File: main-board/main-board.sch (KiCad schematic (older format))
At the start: 68 parts, among them J1 NVIDIA_Jetson_NX_Dev_40pin_Co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, J10 FSESC_6.6_COMM_Minimal, J11 FSESC_6.6_COMM_Minimal, J12 FSESC_6.6_COMM_Minimal, J13 FSESC_6.6_COMM_Minimal, J2 NVIDIA_Jetson_NX_Dev_Button_C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, J3 Conn_01x02, J4 Conn_01x02, J5 Conn_01x02, J6 FSESC_6.6_COMM_Minimal, J7 QWIIC_Generic_Conn, J8 Conn_01x03, J9 FSESC_6.6_COMM_Minimal, M1 Fan_3pin, M2 Fan_3pin, M3 Fan_3pin, Q1 Q_NMOS_GSD, Q2 Q_NMOS_GSD, Q4 Q_NMOS_GSD, Q5 Q_NMOS_GSD, Q6 Q_NMOS_GSD, Q7 Q_NMOS_GSD, Q8 Q_NMOS_GSD, U1 RFM95W_Adafruit_Breakout, U10 Analog Temp Sensor, U11 Adafruit_GPS_V3, U12 SN74AHCT125D, U2 TDK_I3A4W008A033V, U3 TDK_I3A4W008A033V, U5 Teensy_4.1, U6 Analog Temp Sensor, U7 Analog Temp Sensor, U8 Analog Temp Sensor, U9 Analog Temp Sensor

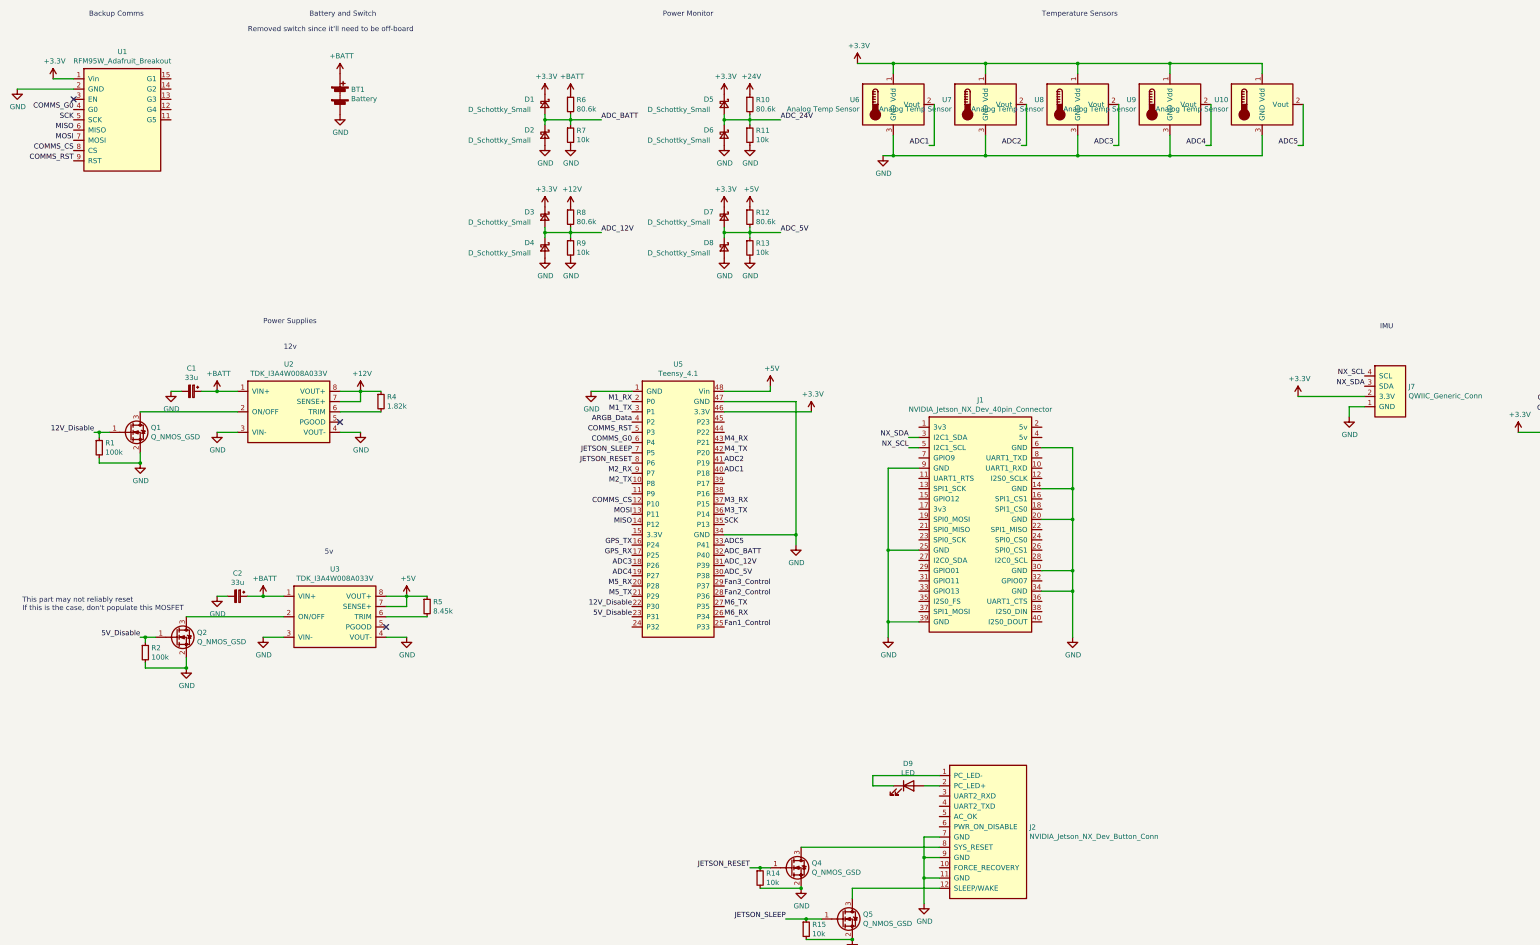
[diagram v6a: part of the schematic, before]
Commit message: Worked on PCB layout
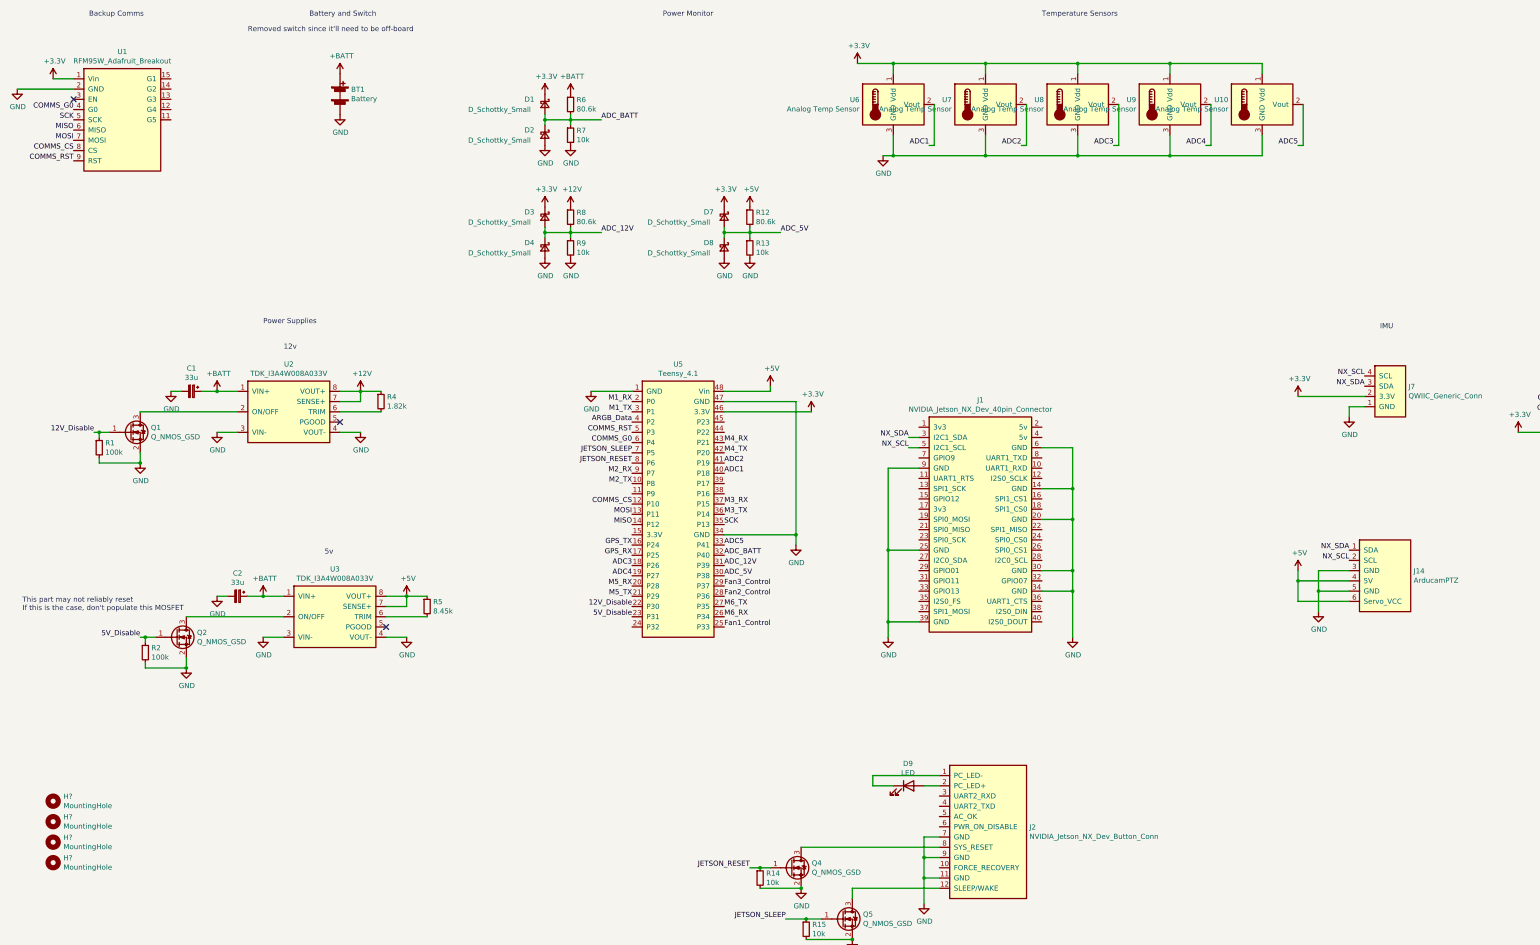
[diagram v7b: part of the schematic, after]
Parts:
- removed D5, D6: D_Schottky_Small, Diode_SMD:D_SOD-323_HandSoldering, symbol Device:D_Schottky_Small
- removed R10: 80.6k, Resistor_SMD:R_0603_1608Metric, symbol Device:R_Small
- removed R11: 10k, Resistor_SMD:R_0603_1608Metric, symbol Device:R_Small
- added H? (x4): MountingHole, MountingHole:MountingHole_3.2mm_M3, symbol Mechanical:MountingHole
- added J14: ArducamPTZ, Connector_JST:JST_XH_B6B-XH-A_1x06_P2.50mm_Vertical, symbol ASTRA_Library:ArducamPTZ
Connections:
- net +5V: now also J14.4 (5V), J14.6 (Servo_VCC)
- net GND: now also J14.3 (GND), J14.5 (GND)
- net NX_SCL: now also J14.2 (SCL)
- net NX_SDA: now also J14.1 (SDA)
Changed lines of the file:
@@
 Wire Wire Line
 	19900 13800 19900 13900
-Text Label 8050 2150 0    50   ~ 0
-ADC_24V
-$Comp
-L Device:R_Small R11
-U 1 1 6119C6A9
-P 7750 2300
-F 0 "R11" H 7809 2346 50  0000 L CNN
-F 1 "10k" H 7809 2255 50  0000 L CNN
-F 2 "Resistor_SMD:R_0603_1608Metric" H 7750 2300 50  0001 C CNN
-F 3 "~" H 7750 2300 50  0001 C CNN
-F 4 "311-10.0KHRCT-ND" H 7750 2300 50  0001 C CNN "Digikey Part Num"
-	1    7750 2300
-	1    0    0    -1
-$EndComp
-$Comp
-L Device:R_Small R10
-U 1 1 6119C6B4
-P 7750 2000
-F 0 "R10" H 7809 2046 50  0000 L CNN
-F 1 "80.6k" H 7809 1955 50  0000 L CNN
-F 2 "Resistor_SMD:R_0603_1608Metric" H 7750 2000 50  0001 C CNN
-F 3 "~" H 7750 2000 50  0001 C CNN
-F 4 "P20500CT-ND" H 7750 2000 50  0001 C CNN "Digikey Part Num"
-	1    7750 2000
-	1    0    0    -1
-$EndComp
-Wire Wire Line
-	8050 2150 7750 2150
-Wire Wire Line
-	7750 2150 7750 2100
-Wire Wire Line
-	7750 2150 7750 2200
-Connection ~ 7750 2150
-$Comp
-L Device:D_Schottky_Small D5
-U 1 1 6119C6C3
-P 7500 2000
-F 0 "D5" V 7450 1800 50  0000 L CNN
-F 1 "D_Schottky_Small" V 7550 1250 50  0000 L CNN
-F 2 "Diode_SMD:D_SOD-323_HandSoldering" V 7500 2000 50  0001 C CNN
-F 3 "~" V 7500 2000 50  0001 C CNN
-F 4 "1514-CMDD6001TRPBFREECT-ND" H 7500 2000 50  0001 C CNN "Digikey Part Num"
-	1    7500 2000
-	0    1    1    0
-$EndComp
-$Comp
-L Device:D_Schottky_Small D6
-U 1 1 6119C6CE
-P 7500 2300
-F 0 "D6" V 7450 2100 50  0000 L CNN
-F 1 "D_Schottky_Small" V 7550 1550 50  0000 L CNN
-F 2 "Diode_SMD:D_SOD-323_HandSoldering" V 7500 2300 50  0001 C CNN
-F 3 "~" V 7500 2300 50  0001 C CNN
-F 4 "1514-CMDD6001TRPBFREECT-ND" H 7500 2300 50  0001 C CNN "Digikey Part Num"
-	1    7500 2300
-	0    1    1    0
-$EndComp
-Wire Wire Line
-	7500 2100 7500 2150
-Wire Wire Line
-	7500 2150 7750 2150
-Wire Wire Line
-	7500 2200 7500 2150
-Connection ~ 7500 2150
-$Comp
-L power:GND #PWR038
-U 1 1 6119C6DC
-P 7750 2400
-F 0 "#PWR038" H 7750 2150 50  0001 C CNN
-F 1 "GND" H 7755 2227 50  0000 C CNN
-F 2 "" H 7750 2400 50  0001 C CNN
-F 3 "" H 7750 2400 50  0001 C CNN
-	1    7750 2400
-	1    0    0    -1
-$EndComp
-$Comp
-L power:GND #PWR034
-U 1 1 6119C6E6
-P 7500 2400
-F 0 "#PWR034" H 7500 2150 50  0001 C CNN
-F 1 "GND" H 7505 2227 50  0000 C CNN
-F 2 "" H 7500 2400 50  0001 C CNN
-F 3 "" H 7500 2400 50  0001 C CNN
-	1    7500 2400
-	1    0    0    -1
-$EndComp
-$Comp
-L power:+3.3V #PWR033
-U 1 1 6119C6F0
-P 7500 1900
-F 0 "#PWR033" H 7500 1750 50  0001 C CNN
-F 1 "+3.3V" H 7515 2073 50  0000 C CNN
-F 2 "" H 7500 1900 50  0001 C CNN
-F 3 "" H 7500 1900 50  0001 C CNN
-	1    7500 1900
-	1    0    0    -1
-$EndComp
-$Comp
-L power:+24V #PWR037
-U 1 1 611B45F0
-P 7750 1900
-F 0 "#PWR037" H 7750 1750 50  0001 C CNN
-F 1 "+24V" H 7765 2073 50  0000 C CNN
-F 2 "" H 7750 1900 50  0001 C CNN
-F 3 "" H 7750 1900 50  0001 C CNN
-	1    7750 1900
-	1    0    0    -1
-$EndComp
 $Comp
 L power:+5V #PWR06
@@
 	1    0    0    -1
 $EndComp
+$Comp
+L ASTRA_Library:ArducamPTZ J14
+U 1 1 612E83D2
+P 13950 6600
+F 0 "J14" H 14228 6646 50  0000 L CNN
+F 1 "ArducamPTZ" H 14228 6555 50  0000 L CNN
+F 2 "Connector_JST:JST_XH_B6B-XH-A_1x06_P2.50mm_Vertical" H 13600 6950 50  0001 C CNN
+F 3 "" H 13600 6950 50  0001 C CNN
+	1    13950 6600
+	1    0    0    -1
+$EndComp
+Text Label 13600 6350 2    50   ~ 0
+NX_SDA
+Text Label 13600 6450 2    50   ~ 0
+NX_SCL
+$Comp
+L power:GND #PWR0101
+U 1 1 612E9CF6
+P 13300 6950
+F 0 "#PWR0101" H 13300 6700 50  0001 C CNN
+F 1 "GND" H 13305 6777 50  0000 C CNN
+F 2 "" H 13300 6950 50  0001 C CNN
+F 3 "" H 13300 6950 50  0001 C CNN
+	1    13300 6950
+	1    0    0    -1
+$EndComp
+$Comp
+L power:+5V #PWR0102
+U 1 1 612FA1AA
+P 13100 6550
+F 0 "#PWR0102" H 13100 6400 50  0001 C CNN
+F 1 "+5V" H 13115 6723 50  0000 C CNN
+F 2 "" H 13100 6550 50  0001 C CNN
+F 3 "" H 13100 6550 50  0001 C CNN
+	1    13100 6550
+	1    0    0    -1
+$EndComp
+Wire Wire Line
+	13300 6950 13300 6750
+Wire Wire Line
+	13300 6550 13600 6550
+Wire Wire Line
+	13600 6650 13100 6650
+Wire Wire Line
+	13100 6650 13100 6550
+Wire Wire Line
+	13600 6850 13100 6850
+Wire Wire Line
+	13100 6850 13100 6650
+Connection ~ 13100 6650
+Wire Wire Line
+	13600 6750 13300 6750
+Connection ~ 13300 6750
+Wire Wire Line
+	13300 6750 13300 6550
+$Comp
+L Mechanical:MountingHole H?
+U 1 1 614879F3
+P 950 8800
+F 0 "H?" H 1050 8846 50  0000 L CNN
+F 1 "MountingHole" H 1050 8755 50  0000 L CNN
+F 2 "MountingHole:MountingHole_3.2mm_M3" H 950 8800 50  0001 C CNN
+F 3 "~" H 950 8800 50  0001 C CNN
+	1    950  8800
+	1    0    0    -1
+$EndComp
+$Comp
+L Mechanical:MountingHole H?
+U 1 1 6148830E
+P 950 9000
+F 0 "H?" H 1050 9046 50  0000 L CNN
+F 1 "MountingHole" H 1050 8955 50  0000 L CNN
+F 2 "MountingHole:MountingHole_3.2mm_M3" H 950 9000 50  0001 C CNN
+F 3 "~" H 950 9000 50  0001 C CNN
+	1    950  9000
+	1    0    0    -1
+$EndComp
+$Comp
+L Mechanical:MountingHole H?
+U 1 1 61488718
+P 950 9200
+F 0 "H?" H 1050 9246 50  0000 L CNN
+F 1 "MountingHole" H 1050 9155 50  0000 L CNN
+F 2 "MountingHole:MountingHole_3.2mm_M3" H 950 9200 50  0001 C CNN
+F 3 "~" H 950 9200 50  0001 C CNN
+	1    950  9200
+	1    0    0    -1
+$EndComp
+$Comp
+L Mechanical:MountingHole H?
+U 1 1 61488957
+P 950 9400
+F 0 "H?" H 1050 9446 50  0000 L CNN
+F 1 "MountingHole" H 1050 9355 50  0000 L CNN
+F 2 "MountingHole:MountingHole_3.2mm_M3" H 950 9400 50  0001 C CNN
+F 3 "~" H 950 9400 50  0001 C CNN
+	1    950  9400
+	1    0    0    -1
+$EndComp

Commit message: Started routing
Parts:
- gave numbers to parts that had none: 4
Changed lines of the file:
@@
 	13300 6750 13300 6550
 $Comp
-L Mechanical:MountingHole H?
+L Mechanical:MountingHole H1
 U 1 1 614879F3
 P 950 8800
-F 0 "H?" H 1050 8846 50  0000 L CNN
+F 0 "H1" H 1050 8846 50  0000 L CNN
 F 1 "MountingHole" H 1050 8755 50  0000 L CNN
 F 2 "MountingHole:MountingHole_3.2mm_M3" H 950 8800 50  0001 C CNN
@@
 $EndComp
 $Comp
-L Mechanical:MountingHole H?
+L Mechanical:MountingHole H2
 U 1 1 6148830E
 P 950 9000
-F 0 "H?" H 1050 9046 50  0000 L CNN
+F 0 "H2" H 1050 9046 50  0000 L CNN
 F 1 "MountingHole" H 1050 8955 50  0000 L CNN
 F 2 "MountingHole:MountingHole_3.2mm_M3" H 950 9000 50  0001 C CNN
@@
 $EndComp
 $Comp
-L Mechanical:MountingHole H?
+L Mechanical:MountingHole H3
 U 1 1 61488718
 P 950 9200
-F 0 "H?" H 1050 9246 50  0000 L CNN
+F 0 "H3" H 1050 9246 50  0000 L CNN
 F 1 "MountingHole" H 1050 9155 50  0000 L CNN
 F 2 "MountingHole:MountingHole_3.2mm_M3" H 950 9200 50  0001 C CNN
@@
 $EndComp
 $Comp
-L Mechanical:MountingHole H?
+L Mechanical:MountingHole H4
 U 1 1 61488957
 P 950 9400
-F 0 "H?" H 1050 9446 50  0000 L CNN
+F 0 "H4" H 1050 9446 50  0000 L CNN
 F 1 "MountingHole" H 1050 9355 50  0000 L CNN
 F 2 "MountingHole:MountingHole_3.2mm_M3" H 950 9400 50  0001 C CNN
